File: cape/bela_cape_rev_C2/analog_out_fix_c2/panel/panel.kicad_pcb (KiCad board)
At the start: 2 copper layers, 48.6 x 22.8 mm, 60 parts, among them J1 Conn_01x03, J2 Conn_01x03

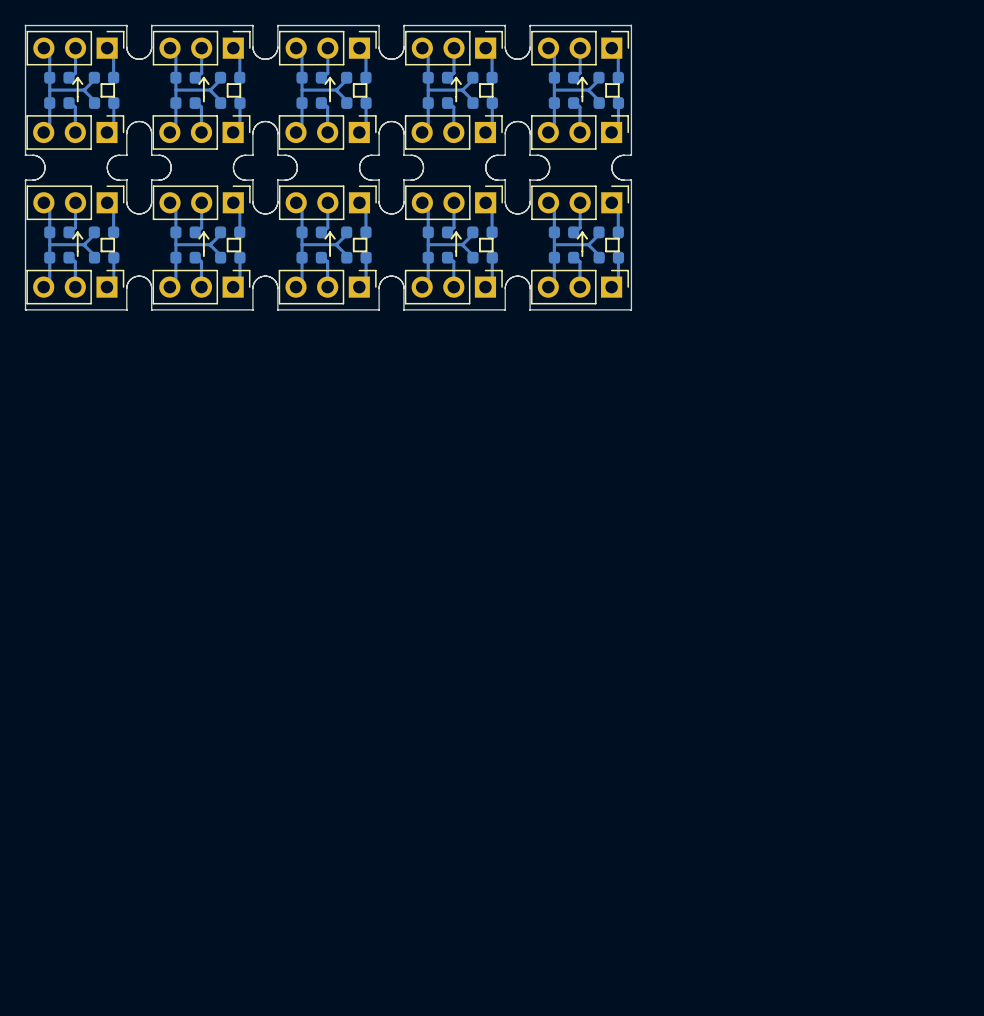
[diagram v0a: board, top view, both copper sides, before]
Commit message: Changed panel to 6x7 with 3mm gap and 0.35mm distance to v-scoring.
(cherry picked from commit ada2b1bb84732b3d844c1010702f27f798faad04)
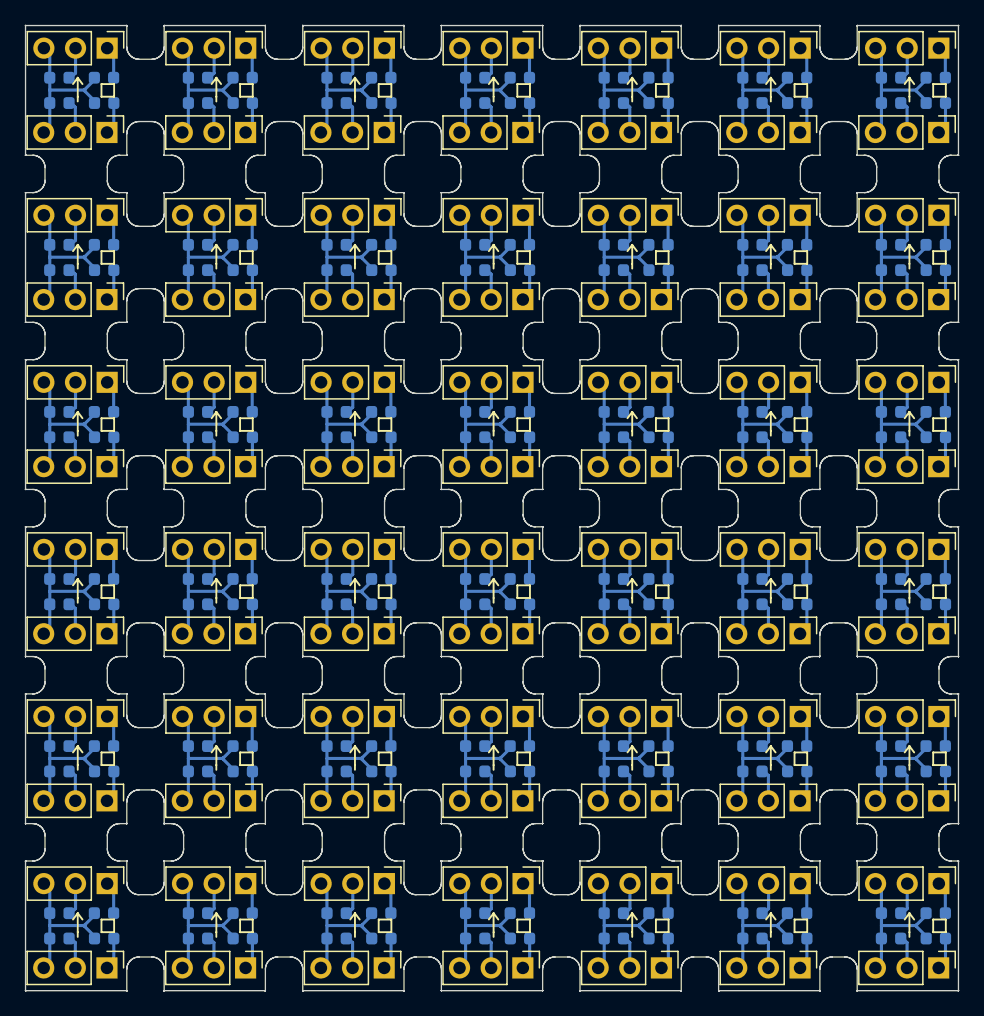
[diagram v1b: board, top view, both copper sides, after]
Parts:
- removed the C1 at (38.0, 33.6)
- removed the C1 at (38.0, 21.2)
- removed the C1 at (27.8, 33.6)
- removed the C1 at (58.2, 33.6)
- removed the C1 at (58.2, 21.2)
- removed the C1 at (48.1, 21.2)
- removed the C1 at (48.1, 33.6)
- removed the C1 at (17.7, 33.6)
- removed the C1 at (27.8, 21.2)
- removed the C2 at (58.2, 31.6)
- removed the C2 at (38.0, 19.2)
- removed the C2 at (48.1, 19.2)
- removed the C2 at (27.8, 31.6)
- removed the C2 at (58.2, 19.2)
- removed the C2 at (48.1, 31.6)
- removed the C2 at (17.7, 31.6)
- removed the C2 at (38.0, 31.6)
- removed the C2 at (27.8, 19.2)
- removed the C3 at (51.7, 21.2)
- removed the C3 at (51.7, 33.6)
- removed the C3 at (41.6, 21.2)
- removed the C3 at (61.8, 21.2)
- removed the C3 at (41.6, 33.6)
- removed the C3 at (31.4, 21.2)
- removed the C3 at (31.4, 33.6)
- removed the C3 at (21.3, 33.6)
- removed the C3 at (61.8, 33.6)
- removed the C4 at (61.8, 31.6)
- removed the C4 at (31.4, 31.6)
- removed the C4 at (51.7, 19.2)
- removed the C4 at (51.7, 31.6)
- removed the C4 at (61.8, 19.2)
- removed the C4 at (41.6, 19.2)
- removed the C4 at (31.4, 19.2)
- removed the C4 at (41.6, 31.6)
- removed the C4 at (21.3, 31.6)
- removed the J1 at (51.9, 36.0)
- removed the J1 at (51.9, 23.6)
- removed the J1 at (31.7, 36.0)
- removed the J1 at (62.1, 23.6)
- removed the J1 at (41.8, 23.6)
- removed the J1 at (31.7, 23.6)
- removed the J1 at (62.1, 36.0)
- removed the J1 at (21.5, 36.0)
- removed the J1 at (41.8, 36.0)
- removed the J2 at (51.9, 16.8)
- removed the J2 at (31.7, 29.2)
- removed the J2 at (41.8, 29.2)
- removed the J2 at (31.7, 16.8)
- removed the J2 at (41.8, 16.8)
- removed the J2 at (51.9, 29.2)
- removed the J2 at (21.6, 29.2)
- removed the J2 at (62.1, 16.8)
- removed the J2 at (62.1, 29.2)
- added C1: 22nF, Capacitor_SMD:C_0603_1608Metric, B.Cu at (84.5, 74.9)
- added C1: 22nF, Capacitor_SMD:C_0603_1608Metric, B.Cu at (28.8, 21.2)
- added C1: 22nF, Capacitor_SMD:C_0603_1608Metric, B.Cu at (84.5, 21.2)
- added C1: 22nF, Capacitor_SMD:C_0603_1608Metric, B.Cu at (51.1, 21.2)
- added C1: 22nF, Capacitor_SMD:C_0603_1608Metric, B.Cu at (73.4, 61.5)
- added C1: 22nF, Capacitor_SMD:C_0603_1608Metric, B.Cu at (17.7, 61.5)
- added C1: 22nF, Capacitor_SMD:C_0603_1608Metric, B.Cu at (40.0, 61.5)
- added C1: 22nF, Capacitor_SMD:C_0603_1608Metric, B.Cu at (17.7, 34.6)
- added C1: 22nF, Capacitor_SMD:C_0603_1608Metric, B.Cu at (62.2, 21.2)
- added C1: 22nF, Capacitor_SMD:C_0603_1608Metric, B.Cu at (51.1, 34.6)
- added C1: 22nF, Capacitor_SMD:C_0603_1608Metric, B.Cu at (40.0, 88.3)
- added C1: 22nF, Capacitor_SMD:C_0603_1608Metric, B.Cu at (40.0, 74.9)
- added C1: 22nF, Capacitor_SMD:C_0603_1608Metric, B.Cu at (73.4, 48.1)
- added C1: 22nF, Capacitor_SMD:C_0603_1608Metric, B.Cu at (28.8, 48.1)
- added C1: 22nF, Capacitor_SMD:C_0603_1608Metric, B.Cu at (84.5, 88.3)
- added C1: 22nF, Capacitor_SMD:C_0603_1608Metric, B.Cu at (51.1, 48.1)
- added C1: 22nF, Capacitor_SMD:C_0603_1608Metric, B.Cu at (62.2, 88.3)
- added C1: 22nF, Capacitor_SMD:C_0603_1608Metric, B.Cu at (73.4, 88.3)
- added C1: 22nF, Capacitor_SMD:C_0603_1608Metric, B.Cu at (28.8, 88.3)
- added C1: 22nF, Capacitor_SMD:C_0603_1608Metric, B.Cu at (62.2, 61.5)
- added C1: 22nF, Capacitor_SMD:C_0603_1608Metric, B.Cu at (73.4, 74.9)
- added C1: 22nF, Capacitor_SMD:C_0603_1608Metric, B.Cu at (17.7, 74.9)
- added C1: 22nF, Capacitor_SMD:C_0603_1608Metric, B.Cu at (84.5, 48.1)
- added C1: 22nF, Capacitor_SMD:C_0603_1608Metric, B.Cu at (51.1, 61.5)
- added C1: 22nF, Capacitor_SMD:C_0603_1608Metric, B.Cu at (62.2, 74.9)
- added C1: 22nF, Capacitor_SMD:C_0603_1608Metric, B.Cu at (40.0, 34.6)
- added C1: 22nF, Capacitor_SMD:C_0603_1608Metric, B.Cu at (84.5, 34.6)
- added C1: 22nF, Capacitor_SMD:C_0603_1608Metric, B.Cu at (62.2, 48.1)
- added C1: 22nF, Capacitor_SMD:C_0603_1608Metric, B.Cu at (17.7, 48.1)
- added C1: 22nF, Capacitor_SMD:C_0603_1608Metric, B.Cu at (28.8, 74.9)
- added C1: 22nF, Capacitor_SMD:C_0603_1608Metric, B.Cu at (62.2, 34.6)
- added C1: 22nF, Capacitor_SMD:C_0603_1608Metric, B.Cu at (73.4, 34.6)
- added C1: 22nF, Capacitor_SMD:C_0603_1608Metric, B.Cu at (28.8, 61.5)
- added C1: 22nF, Capacitor_SMD:C_0603_1608Metric, B.Cu at (73.4, 21.2)
- added C1: 22nF, Capacitor_SMD:C_0603_1608Metric, B.Cu at (17.7, 88.3)
- added C1: 22nF, Capacitor_SMD:C_0603_1608Metric, B.Cu at (51.1, 74.9)
- added C1: 22nF, Capacitor_SMD:C_0603_1608Metric, B.Cu at (40.0, 48.1)
- added C1: 22nF, Capacitor_SMD:C_0603_1608Metric, B.Cu at (84.5, 61.5)
- added C1: 22nF, Capacitor_SMD:C_0603_1608Metric, B.Cu at (40.0, 21.2)
- added C1: 22nF, Capacitor_SMD:C_0603_1608Metric, B.Cu at (28.8, 34.6)
- added C1: 22nF, Capacitor_SMD:C_0603_1608Metric, B.Cu at (51.1, 88.3)
- added C2: 22nF, Capacitor_SMD:C_0603_1608Metric, B.Cu at (84.5, 86.3)
- added C2: 22nF, Capacitor_SMD:C_0603_1608Metric, B.Cu at (51.1, 72.8)
- added C2: 22nF, Capacitor_SMD:C_0603_1608Metric, B.Cu at (28.8, 86.3)
- added C2: 22nF, Capacitor_SMD:C_0603_1608Metric, B.Cu at (17.7, 32.6)
- added C2: 22nF, Capacitor_SMD:C_0603_1608Metric, B.Cu at (40.0, 32.6)
- added C2: 22nF, Capacitor_SMD:C_0603_1608Metric, B.Cu at (73.4, 59.4)
- added C2: 22nF, Capacitor_SMD:C_0603_1608Metric, B.Cu at (17.7, 72.8)
- added C2: 22nF, Capacitor_SMD:C_0603_1608Metric, B.Cu at (84.5, 59.4)
- added C2: 22nF, Capacitor_SMD:C_0603_1608Metric, B.Cu at (62.2, 32.6)
- added C2: 22nF, Capacitor_SMD:C_0603_1608Metric, B.Cu at (62.2, 72.8)
- added C2: 22nF, Capacitor_SMD:C_0603_1608Metric, B.Cu at (62.2, 46.0)
- added C2: 22nF, Capacitor_SMD:C_0603_1608Metric, B.Cu at (28.8, 19.2)
- added C2: 22nF, Capacitor_SMD:C_0603_1608Metric, B.Cu at (84.5, 46.0)
- added C2: 22nF, Capacitor_SMD:C_0603_1608Metric, B.Cu at (84.5, 72.8)
- added C2: 22nF, Capacitor_SMD:C_0603_1608Metric, B.Cu at (51.1, 86.3)
- added C2: 22nF, Capacitor_SMD:C_0603_1608Metric, B.Cu at (17.7, 86.3)
- added C2: 22nF, Capacitor_SMD:C_0603_1608Metric, B.Cu at (73.4, 72.8)
- added C2: 22nF, Capacitor_SMD:C_0603_1608Metric, B.Cu at (28.8, 46.0)
- added C2: 22nF, Capacitor_SMD:C_0603_1608Metric, B.Cu at (28.8, 59.4)
- added C2: 22nF, Capacitor_SMD:C_0603_1608Metric, B.Cu at (40.0, 19.2)
- added C2: 22nF, Capacitor_SMD:C_0603_1608Metric, B.Cu at (73.4, 32.6)
- added C2: 22nF, Capacitor_SMD:C_0603_1608Metric, B.Cu at (51.1, 19.2)
- added C2: 22nF, Capacitor_SMD:C_0603_1608Metric, B.Cu at (51.1, 46.0)
- added C2: 22nF, Capacitor_SMD:C_0603_1608Metric, B.Cu at (62.2, 86.3)
- added C2: 22nF, Capacitor_SMD:C_0603_1608Metric, B.Cu at (84.5, 19.2)
- added C2: 22nF, Capacitor_SMD:C_0603_1608Metric, B.Cu at (17.7, 46.0)
- added C2: 22nF, Capacitor_SMD:C_0603_1608Metric, B.Cu at (40.0, 46.0)
- added C2: 22nF, Capacitor_SMD:C_0603_1608Metric, B.Cu at (28.8, 72.8)
- added C2: 22nF, Capacitor_SMD:C_0603_1608Metric, B.Cu at (17.7, 59.4)
- added C2: 22nF, Capacitor_SMD:C_0603_1608Metric, B.Cu at (84.5, 32.6)
- added C2: 22nF, Capacitor_SMD:C_0603_1608Metric, B.Cu at (62.2, 59.4)
- added C2: 22nF, Capacitor_SMD:C_0603_1608Metric, B.Cu at (73.4, 46.0)
- added C2: 22nF, Capacitor_SMD:C_0603_1608Metric, B.Cu at (51.1, 59.4)
- added C2: 22nF, Capacitor_SMD:C_0603_1608Metric, B.Cu at (73.4, 86.3)
- added C2: 22nF, Capacitor_SMD:C_0603_1608Metric, B.Cu at (40.0, 86.3)
- added C2: 22nF, Capacitor_SMD:C_0603_1608Metric, B.Cu at (62.2, 19.2)
- added C2: 22nF, Capacitor_SMD:C_0603_1608Metric, B.Cu at (40.0, 59.4)
- added C2: 22nF, Capacitor_SMD:C_0603_1608Metric, B.Cu at (28.8, 32.6)
- added C2: 22nF, Capacitor_SMD:C_0603_1608Metric, B.Cu at (40.0, 72.8)
- added C2: 22nF, Capacitor_SMD:C_0603_1608Metric, B.Cu at (73.4, 19.2)
- added C2: 22nF, Capacitor_SMD:C_0603_1608Metric, B.Cu at (51.1, 32.6)
- added C3: 22nF, Capacitor_SMD:C_0603_1608Metric, B.Cu at (88.1, 21.2)
- added C3: 22nF, Capacitor_SMD:C_0603_1608Metric, B.Cu at (88.1, 61.5)
- added C3: 22nF, Capacitor_SMD:C_0603_1608Metric, B.Cu at (21.3, 48.1)
- added C3: 22nF, Capacitor_SMD:C_0603_1608Metric, B.Cu at (88.1, 48.1)
- added C3: 22nF, Capacitor_SMD:C_0603_1608Metric, B.Cu at (54.7, 88.3)
- added C3: 22nF, Capacitor_SMD:C_0603_1608Metric, B.Cu at (88.1, 88.3)
- added C3: 22nF, Capacitor_SMD:C_0603_1608Metric, B.Cu at (54.7, 21.2)
- added C3: 22nF, Capacitor_SMD:C_0603_1608Metric, B.Cu at (88.1, 74.9)
- added C3: 22nF, Capacitor_SMD:C_0603_1608Metric, B.Cu at (54.7, 74.9)
- added C3: 22nF, Capacitor_SMD:C_0603_1608Metric, B.Cu at (32.4, 61.5)
- added C3: 22nF, Capacitor_SMD:C_0603_1608Metric, B.Cu at (43.6, 61.5)
- added C3: 22nF, Capacitor_SMD:C_0603_1608Metric, B.Cu at (43.6, 48.1)
- added C3: 22nF, Capacitor_SMD:C_0603_1608Metric, B.Cu at (21.3, 88.3)
- added C3: 22nF, Capacitor_SMD:C_0603_1608Metric, B.Cu at (65.8, 61.5)
- added C3: 22nF, Capacitor_SMD:C_0603_1608Metric, B.Cu at (65.8, 48.1)
- added C3: 22nF, Capacitor_SMD:C_0603_1608Metric, B.Cu at (32.4, 48.1)
- added C3: 22nF, Capacitor_SMD:C_0603_1608Metric, B.Cu at (54.7, 61.5)
- added C3: 22nF, Capacitor_SMD:C_0603_1608Metric, B.Cu at (88.1, 34.6)
- added C3: 22nF, Capacitor_SMD:C_0603_1608Metric, B.Cu at (32.4, 21.2)
- added C3: 22nF, Capacitor_SMD:C_0603_1608Metric, B.Cu at (43.6, 34.6)
- added C3: 22nF, Capacitor_SMD:C_0603_1608Metric, B.Cu at (21.3, 74.9)
- added C3: 22nF, Capacitor_SMD:C_0603_1608Metric, B.Cu at (32.4, 74.9)
- added C3: 22nF, Capacitor_SMD:C_0603_1608Metric, B.Cu at (21.3, 34.6)
- added C3: 22nF, Capacitor_SMD:C_0603_1608Metric, B.Cu at (54.7, 48.1)
- added C3: 22nF, Capacitor_SMD:C_0603_1608Metric, B.Cu at (43.6, 74.9)
- added C3: 22nF, Capacitor_SMD:C_0603_1608Metric, B.Cu at (43.6, 88.3)
- added C3: 22nF, Capacitor_SMD:C_0603_1608Metric, B.Cu at (65.8, 74.9)
- added C3: 22nF, Capacitor_SMD:C_0603_1608Metric, B.Cu at (43.6, 21.2)
- added C3: 22nF, Capacitor_SMD:C_0603_1608Metric, B.Cu at (65.8, 34.6)
- added C3: 22nF, Capacitor_SMD:C_0603_1608Metric, B.Cu at (54.7, 34.6)
- added C3: 22nF, Capacitor_SMD:C_0603_1608Metric, B.Cu at (77.0, 61.5)
- added C3: 22nF, Capacitor_SMD:C_0603_1608Metric, B.Cu at (77.0, 48.1)
- added C3: 22nF, Capacitor_SMD:C_0603_1608Metric, B.Cu at (65.8, 21.2)
- added C3: 22nF, Capacitor_SMD:C_0603_1608Metric, B.Cu at (32.4, 34.6)
- added C3: 22nF, Capacitor_SMD:C_0603_1608Metric, B.Cu at (77.0, 74.9)
- added C3: 22nF, Capacitor_SMD:C_0603_1608Metric, B.Cu at (21.3, 61.5)
- added C3: 22nF, Capacitor_SMD:C_0603_1608Metric, B.Cu at (32.4, 88.3)
- added C3: 22nF, Capacitor_SMD:C_0603_1608Metric, B.Cu at (77.0, 34.6)
- added C3: 22nF, Capacitor_SMD:C_0603_1608Metric, B.Cu at (77.0, 88.3)
- added C3: 22nF, Capacitor_SMD:C_0603_1608Metric, B.Cu at (65.8, 88.3)
- added C3: 22nF, Capacitor_SMD:C_0603_1608Metric, B.Cu at (77.0, 21.2)
- added C4: 22nF, Capacitor_SMD:C_0603_1608Metric, B.Cu at (32.4, 32.6)
- added C4: 22nF, Capacitor_SMD:C_0603_1608Metric, B.Cu at (88.1, 86.3)
- added C4: 22nF, Capacitor_SMD:C_0603_1608Metric, B.Cu at (43.6, 32.6)
- added C4: 22nF, Capacitor_SMD:C_0603_1608Metric, B.Cu at (43.6, 46.0)
- added C4: 22nF, Capacitor_SMD:C_0603_1608Metric, B.Cu at (65.8, 72.8)
- added C4: 22nF, Capacitor_SMD:C_0603_1608Metric, B.Cu at (54.7, 72.8)
- added C4: 22nF, Capacitor_SMD:C_0603_1608Metric, B.Cu at (21.3, 72.8)
- added C4: 22nF, Capacitor_SMD:C_0603_1608Metric, B.Cu at (88.1, 46.0)
- added C4: 22nF, Capacitor_SMD:C_0603_1608Metric, B.Cu at (21.3, 32.6)
- added C4: 22nF, Capacitor_SMD:C_0603_1608Metric, B.Cu at (32.4, 86.3)
- added C4: 22nF, Capacitor_SMD:C_0603_1608Metric, B.Cu at (54.7, 19.2)
- added C4: 22nF, Capacitor_SMD:C_0603_1608Metric, B.Cu at (43.6, 72.8)
- added C4: 22nF, Capacitor_SMD:C_0603_1608Metric, B.Cu at (76.9, 32.6)
- added C4: 22nF, Capacitor_SMD:C_0603_1608Metric, B.Cu at (43.6, 86.3)
- added C4: 22nF, Capacitor_SMD:C_0603_1608Metric, B.Cu at (76.9, 86.3)
- added C4: 22nF, Capacitor_SMD:C_0603_1608Metric, B.Cu at (43.6, 59.4)
- added C4: 22nF, Capacitor_SMD:C_0603_1608Metric, B.Cu at (32.4, 19.2)
- added C4: 22nF, Capacitor_SMD:C_0603_1608Metric, B.Cu at (32.4, 59.4)
- added C4: 22nF, Capacitor_SMD:C_0603_1608Metric, B.Cu at (54.7, 86.3)
- added C4: 22nF, Capacitor_SMD:C_0603_1608Metric, B.Cu at (65.8, 86.3)
- added C4: 22nF, Capacitor_SMD:C_0603_1608Metric, B.Cu at (54.7, 59.4)
- added C4: 22nF, Capacitor_SMD:C_0603_1608Metric, B.Cu at (88.1, 72.8)
- added C4: 22nF, Capacitor_SMD:C_0603_1608Metric, B.Cu at (76.9, 19.2)
- added C4: 22nF, Capacitor_SMD:C_0603_1608Metric, B.Cu at (21.3, 86.3)
- added C4: 22nF, Capacitor_SMD:C_0603_1608Metric, B.Cu at (65.8, 19.2)
- added C4: 22nF, Capacitor_SMD:C_0603_1608Metric, B.Cu at (32.4, 46.0)
- added C4: 22nF, Capacitor_SMD:C_0603_1608Metric, B.Cu at (65.8, 46.0)
- added C4: 22nF, Capacitor_SMD:C_0603_1608Metric, B.Cu at (88.1, 19.2)
- added C4: 22nF, Capacitor_SMD:C_0603_1608Metric, B.Cu at (65.8, 59.4)
- added C4: 22nF, Capacitor_SMD:C_0603_1608Metric, B.Cu at (21.3, 46.0)
- added C4: 22nF, Capacitor_SMD:C_0603_1608Metric, B.Cu at (32.4, 72.8)
- added C4: 22nF, Capacitor_SMD:C_0603_1608Metric, B.Cu at (76.9, 72.8)
- added C4: 22nF, Capacitor_SMD:C_0603_1608Metric, B.Cu at (76.9, 46.0)
- added C4: 22nF, Capacitor_SMD:C_0603_1608Metric, B.Cu at (21.3, 59.4)
- added C4: 22nF, Capacitor_SMD:C_0603_1608Metric, B.Cu at (65.8, 32.6)
- added C4: 22nF, Capacitor_SMD:C_0603_1608Metric, B.Cu at (88.1, 59.4)
- added C4: 22nF, Capacitor_SMD:C_0603_1608Metric, B.Cu at (54.7, 46.0)
- added C4: 22nF, Capacitor_SMD:C_0603_1608Metric, B.Cu at (43.6, 19.2)
- added C4: 22nF, Capacitor_SMD:C_0603_1608Metric, B.Cu at (76.9, 59.4)
- added C4: 22nF, Capacitor_SMD:C_0603_1608Metric, B.Cu at (54.7, 32.6)
- added C4: 22nF, Capacitor_SMD:C_0603_1608Metric, B.Cu at (88.1, 32.6)
- added J1: Conn_01x03, Connector_PinHeader_2.54mm:PinHeader_1x03_P2.54mm_Vertical, F.Cu at (32.7, 77.2)
- added J1: Conn_01x03, Connector_PinHeader_2.54mm:PinHeader_1x03_P2.54mm_Vertical, F.Cu at (43.8, 77.2)
- added J1: Conn_01x03, Connector_PinHeader_2.54mm:PinHeader_1x03_P2.54mm_Vertical, F.Cu at (66.1, 37.0)
- added J1: Conn_01x03, Connector_PinHeader_2.54mm:PinHeader_1x03_P2.54mm_Vertical, F.Cu at (32.7, 50.4)
- added J1: Conn_01x03, Connector_PinHeader_2.54mm:PinHeader_1x03_P2.54mm_Vertical, F.Cu at (88.3, 23.6)
- added J1: Conn_01x03, Connector_PinHeader_2.54mm:PinHeader_1x03_P2.54mm_Vertical, F.Cu at (54.9, 50.4)
- added J1: Conn_01x03, Connector_PinHeader_2.54mm:PinHeader_1x03_P2.54mm_Vertical, F.Cu at (77.2, 23.6)
- added J1: Conn_01x03, Connector_PinHeader_2.54mm:PinHeader_1x03_P2.54mm_Vertical, F.Cu at (88.3, 37.0)
- added J1: Conn_01x03, Connector_PinHeader_2.54mm:PinHeader_1x03_P2.54mm_Vertical, F.Cu at (43.8, 50.4)
- added J1: Conn_01x03, Connector_PinHeader_2.54mm:PinHeader_1x03_P2.54mm_Vertical, F.Cu at (66.1, 90.7)
- added J1: Conn_01x03, Connector_PinHeader_2.54mm:PinHeader_1x03_P2.54mm_Vertical, F.Cu at (66.1, 23.6)
- added J1: Conn_01x03, Connector_PinHeader_2.54mm:PinHeader_1x03_P2.54mm_Vertical, F.Cu at (21.5, 77.2)
- added J1: Conn_01x03, Connector_PinHeader_2.54mm:PinHeader_1x03_P2.54mm_Vertical, F.Cu at (66.1, 63.8)
- added J1: Conn_01x03, Connector_PinHeader_2.54mm:PinHeader_1x03_P2.54mm_Vertical, F.Cu at (77.2, 77.2)
- added J1: Conn_01x03, Connector_PinHeader_2.54mm:PinHeader_1x03_P2.54mm_Vertical, F.Cu at (88.3, 63.8)
- added J1: Conn_01x03, Connector_PinHeader_2.54mm:PinHeader_1x03_P2.54mm_Vertical, F.Cu at (66.1, 50.4)
- added J1: Conn_01x03, Connector_PinHeader_2.54mm:PinHeader_1x03_P2.54mm_Vertical, F.Cu at (77.2, 63.8)
- added J1: Conn_01x03, Connector_PinHeader_2.54mm:PinHeader_1x03_P2.54mm_Vertical, F.Cu at (77.2, 50.4)
- added J1: Conn_01x03, Connector_PinHeader_2.54mm:PinHeader_1x03_P2.54mm_Vertical, F.Cu at (77.2, 90.7)
- added J1: Conn_01x03, Connector_PinHeader_2.54mm:PinHeader_1x03_P2.54mm_Vertical, F.Cu at (88.3, 90.7)
- added J1: Conn_01x03, Connector_PinHeader_2.54mm:PinHeader_1x03_P2.54mm_Vertical, F.Cu at (54.9, 77.2)
- added J1: Conn_01x03, Connector_PinHeader_2.54mm:PinHeader_1x03_P2.54mm_Vertical, F.Cu at (54.9, 63.8)
- added J1: Conn_01x03, Connector_PinHeader_2.54mm:PinHeader_1x03_P2.54mm_Vertical, F.Cu at (21.5, 37.0)
- added J1: Conn_01x03, Connector_PinHeader_2.54mm:PinHeader_1x03_P2.54mm_Vertical, F.Cu at (21.5, 63.8)
- added J1: Conn_01x03, Connector_PinHeader_2.54mm:PinHeader_1x03_P2.54mm_Vertical, F.Cu at (21.5, 50.4)
- added J1: Conn_01x03, Connector_PinHeader_2.54mm:PinHeader_1x03_P2.54mm_Vertical, F.Cu at (43.8, 90.7)
- added J1: Conn_01x03, Connector_PinHeader_2.54mm:PinHeader_1x03_P2.54mm_Vertical, F.Cu at (54.9, 90.7)
- added J1: Conn_01x03, Connector_PinHeader_2.54mm:PinHeader_1x03_P2.54mm_Vertical, F.Cu at (88.3, 50.4)
- added J1: Conn_01x03, Connector_PinHeader_2.54mm:PinHeader_1x03_P2.54mm_Vertical, F.Cu at (32.7, 23.6)
- added J1: Conn_01x03, Connector_PinHeader_2.54mm:PinHeader_1x03_P2.54mm_Vertical, F.Cu at (32.7, 90.7)
- added J1: Conn_01x03, Connector_PinHeader_2.54mm:PinHeader_1x03_P2.54mm_Vertical, F.Cu at (32.7, 63.8)
- added J1: Conn_01x03, Connector_PinHeader_2.54mm:PinHeader_1x03_P2.54mm_Vertical, F.Cu at (43.8, 23.6)
- added J1: Conn_01x03, Connector_PinHeader_2.54mm:PinHeader_1x03_P2.54mm_Vertical, F.Cu at (66.1, 77.2)
- added J1: Conn_01x03, Connector_PinHeader_2.54mm:PinHeader_1x03_P2.54mm_Vertical, F.Cu at (88.3, 77.2)
- added J1: Conn_01x03, Connector_PinHeader_2.54mm:PinHeader_1x03_P2.54mm_Vertical, F.Cu at (43.8, 37.0)
- added J1: Conn_01x03, Connector_PinHeader_2.54mm:PinHeader_1x03_P2.54mm_Vertical, F.Cu at (43.8, 63.8)
- added J1: Conn_01x03, Connector_PinHeader_2.54mm:PinHeader_1x03_P2.54mm_Vertical, F.Cu at (77.2, 37.0)
- added J1: Conn_01x03, Connector_PinHeader_2.54mm:PinHeader_1x03_P2.54mm_Vertical, F.Cu at (32.7, 37.0)
- added J1: Conn_01x03, Connector_PinHeader_2.54mm:PinHeader_1x03_P2.54mm_Vertical, F.Cu at (54.9, 23.6)
- added J1: Conn_01x03, Connector_PinHeader_2.54mm:PinHeader_1x03_P2.54mm_Vertical, F.Cu at (54.9, 37.0)
- added J1: Conn_01x03, Connector_PinHeader_2.54mm:PinHeader_1x03_P2.54mm_Vertical, F.Cu at (21.5, 90.7)
- added J2: Conn_01x03, Connector_PinHeader_2.54mm:PinHeader_1x03_P2.54mm_Vertical, F.Cu at (21.6, 57.1)
- added J2: Conn_01x03, Connector_PinHeader_2.54mm:PinHeader_1x03_P2.54mm_Vertical, F.Cu at (32.7, 70.5)
- added J2: Conn_01x03, Connector_PinHeader_2.54mm:PinHeader_1x03_P2.54mm_Vertical, F.Cu at (77.2, 16.8)
- added J2: Conn_01x03, Connector_PinHeader_2.54mm:PinHeader_1x03_P2.54mm_Vertical, F.Cu at (21.6, 30.2)
- added J2: Conn_01x03, Connector_PinHeader_2.54mm:PinHeader_1x03_P2.54mm_Vertical, F.Cu at (32.7, 57.1)
- added J2: Conn_01x03, Connector_PinHeader_2.54mm:PinHeader_1x03_P2.54mm_Vertical, F.Cu at (32.7, 16.8)
- added J2: Conn_01x03, Connector_PinHeader_2.54mm:PinHeader_1x03_P2.54mm_Vertical, F.Cu at (88.3, 43.6)
- added J2: Conn_01x03, Connector_PinHeader_2.54mm:PinHeader_1x03_P2.54mm_Vertical, F.Cu at (32.7, 43.6)
- added J2: Conn_01x03, Connector_PinHeader_2.54mm:PinHeader_1x03_P2.54mm_Vertical, F.Cu at (66.1, 43.6)
- added J2: Conn_01x03, Connector_PinHeader_2.54mm:PinHeader_1x03_P2.54mm_Vertical, F.Cu at (43.8, 83.9)
- added J2: Conn_01x03, Connector_PinHeader_2.54mm:PinHeader_1x03_P2.54mm_Vertical, F.Cu at (32.7, 30.2)
- added J2: Conn_01x03, Connector_PinHeader_2.54mm:PinHeader_1x03_P2.54mm_Vertical, F.Cu at (88.3, 30.2)
- added J2: Conn_01x03, Connector_PinHeader_2.54mm:PinHeader_1x03_P2.54mm_Vertical, F.Cu at (88.3, 57.1)
- added J2: Conn_01x03, Connector_PinHeader_2.54mm:PinHeader_1x03_P2.54mm_Vertical, F.Cu at (77.2, 83.9)
- added J2: Conn_01x03, Connector_PinHeader_2.54mm:PinHeader_1x03_P2.54mm_Vertical, F.Cu at (54.9, 43.6)
- added J2: Conn_01x03, Connector_PinHeader_2.54mm:PinHeader_1x03_P2.54mm_Vertical, F.Cu at (21.6, 43.6)
- added J2: Conn_01x03, Connector_PinHeader_2.54mm:PinHeader_1x03_P2.54mm_Vertical, F.Cu at (66.1, 70.5)
- added J2: Conn_01x03, Connector_PinHeader_2.54mm:PinHeader_1x03_P2.54mm_Vertical, F.Cu at (77.2, 57.1)
- added J2: Conn_01x03, Connector_PinHeader_2.54mm:PinHeader_1x03_P2.54mm_Vertical, F.Cu at (77.2, 70.5)
- added J2: Conn_01x03, Connector_PinHeader_2.54mm:PinHeader_1x03_P2.54mm_Vertical, F.Cu at (43.8, 43.6)
- added J2: Conn_01x03, Connector_PinHeader_2.54mm:PinHeader_1x03_P2.54mm_Vertical, F.Cu at (21.6, 70.5)
- added J2: Conn_01x03, Connector_PinHeader_2.54mm:PinHeader_1x03_P2.54mm_Vertical, F.Cu at (54.9, 83.9)
- added J2: Conn_01x03, Connector_PinHeader_2.54mm:PinHeader_1x03_P2.54mm_Vertical, F.Cu at (88.3, 16.8)
- added J2: Conn_01x03, Connector_PinHeader_2.54mm:PinHeader_1x03_P2.54mm_Vertical, F.Cu at (77.2, 30.2)
- added J2: Conn_01x03, Connector_PinHeader_2.54mm:PinHeader_1x03_P2.54mm_Vertical, F.Cu at (54.9, 70.5)
- added J2: Conn_01x03, Connector_PinHeader_2.54mm:PinHeader_1x03_P2.54mm_Vertical, F.Cu at (88.3, 70.5)
- added J2: Conn_01x03, Connector_PinHeader_2.54mm:PinHeader_1x03_P2.54mm_Vertical, F.Cu at (43.8, 57.1)
- added J2: Conn_01x03, Connector_PinHeader_2.54mm:PinHeader_1x03_P2.54mm_Vertical, F.Cu at (43.8, 70.5)
- added J2: Conn_01x03, Connector_PinHeader_2.54mm:PinHeader_1x03_P2.54mm_Vertical, F.Cu at (54.9, 57.1)
- added J2: Conn_01x03, Connector_PinHeader_2.54mm:PinHeader_1x03_P2.54mm_Vertical, F.Cu at (66.1, 57.1)
- added J2: Conn_01x03, Connector_PinHeader_2.54mm:PinHeader_1x03_P2.54mm_Vertical, F.Cu at (54.9, 30.2)
- added J2: Conn_01x03, Connector_PinHeader_2.54mm:PinHeader_1x03_P2.54mm_Vertical, F.Cu at (66.1, 30.2)
- added J2: Conn_01x03, Connector_PinHeader_2.54mm:PinHeader_1x03_P2.54mm_Vertical, F.Cu at (66.1, 83.9)
- added J2: Conn_01x03, Connector_PinHeader_2.54mm:PinHeader_1x03_P2.54mm_Vertical, F.Cu at (66.1, 16.8)
- added J2: Conn_01x03, Connector_PinHeader_2.54mm:PinHeader_1x03_P2.54mm_Vertical, F.Cu at (32.7, 83.9)
- added J2: Conn_01x03, Connector_PinHeader_2.54mm:PinHeader_1x03_P2.54mm_Vertical, F.Cu at (77.2, 43.6)
- added J2: Conn_01x03, Connector_PinHeader_2.54mm:PinHeader_1x03_P2.54mm_Vertical, F.Cu at (88.3, 83.9)
- added J2: Conn_01x03, Connector_PinHeader_2.54mm:PinHeader_1x03_P2.54mm_Vertical, F.Cu at (43.8, 30.2)
- added J2: Conn_01x03, Connector_PinHeader_2.54mm:PinHeader_1x03_P2.54mm_Vertical, F.Cu at (21.6, 83.9)
- added J2: Conn_01x03, Connector_PinHeader_2.54mm:PinHeader_1x03_P2.54mm_Vertical, F.Cu at (43.8, 16.8)
- added J2: Conn_01x03, Connector_PinHeader_2.54mm:PinHeader_1x03_P2.54mm_Vertical, F.Cu at (54.9, 16.8)
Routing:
- net Board_31-GND: track 0.00 -> 12.8 mm
- net Board_30-GND: track 0.00 -> 12.8 mm
- net Board_29-GND: track 0.00 -> 12.8 mm
- net Board_28-GND: track 0.00 -> 12.8 mm
- net Board_32-GND: track 0.00 -> 12.8 mm
- net Board_10-GND: track 0.00 -> 12.8 mm
- net Board_33-GND: track 0.00 -> 12.8 mm
- net Board_17-GND: track 0.00 -> 12.8 mm
- net Board_16-GND: track 0.00 -> 12.8 mm
- net Board_11-GND: track 0.00 -> 12.8 mm
- net Board_38-GND: track 0.00 -> 12.8 mm
- net Board_34-GND: track 0.00 -> 12.8 mm
- net Board_37-GND: track 0.00 -> 12.8 mm
- net Board_18-GND: track 0.00 -> 12.8 mm
- net Board_35-GND: track 0.00 -> 12.8 mm
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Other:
- board size 48.6 x 22.8 mm -> 74.9 x 77.5 mm
